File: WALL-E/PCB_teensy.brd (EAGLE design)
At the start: 92.8 x 115.8 mm, 44 parts

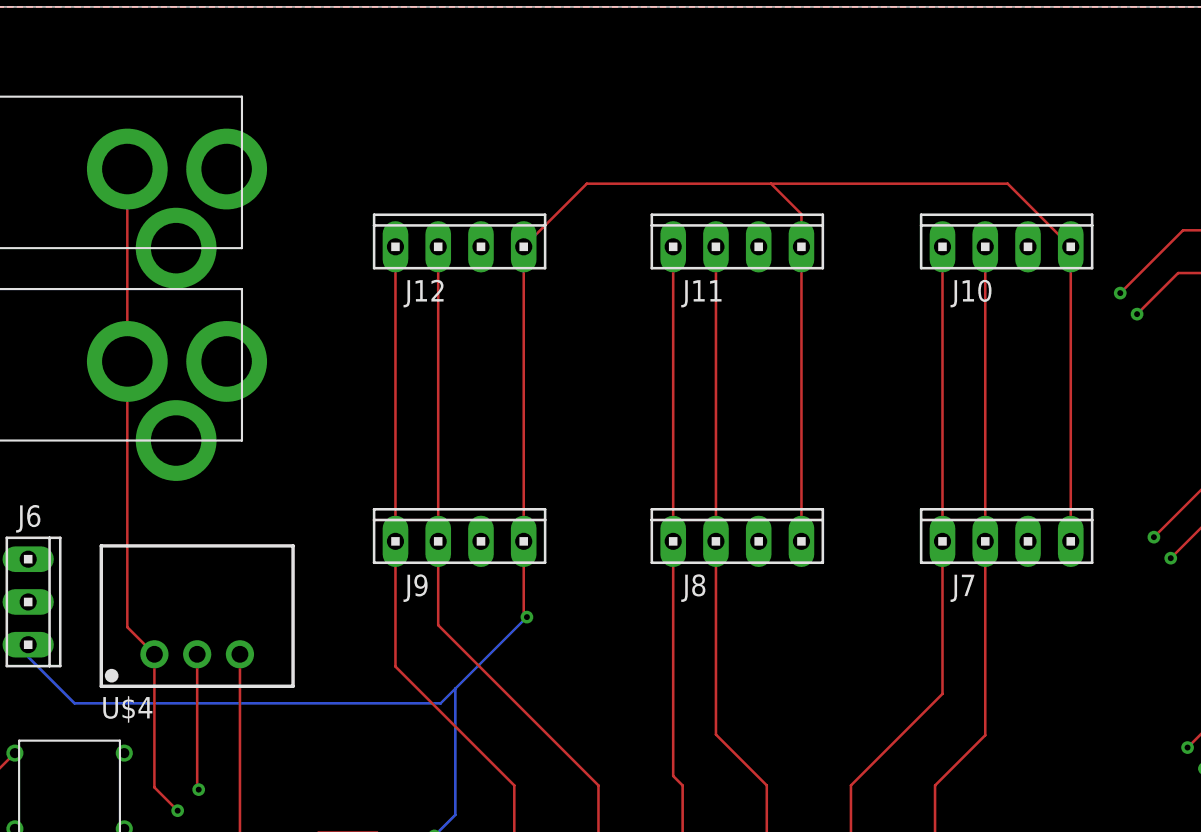
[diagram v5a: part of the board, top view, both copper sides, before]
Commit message: added silkscreen to i2c headers
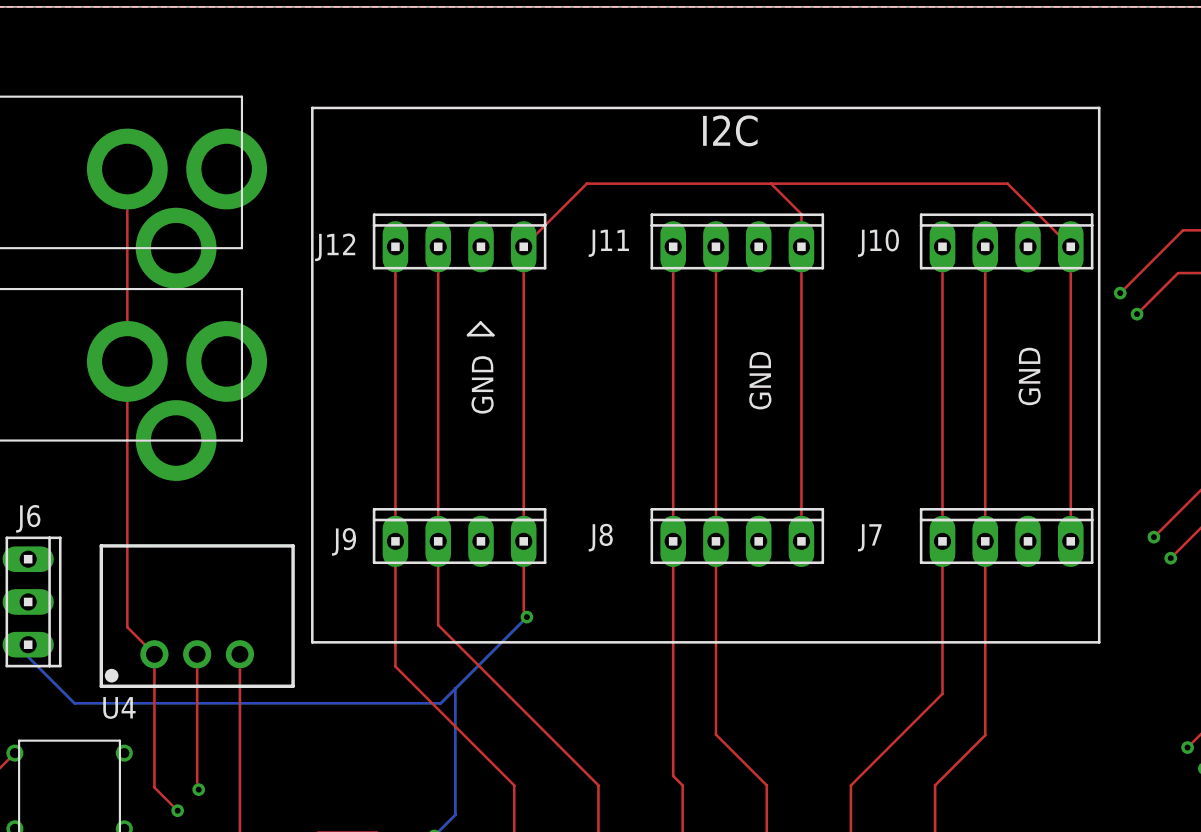
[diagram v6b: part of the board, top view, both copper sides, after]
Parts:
- renumbered U$4 to U4
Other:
- board text added: "I2C"
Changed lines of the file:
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@@
 <text x="4" y="81" size="1.016" layer="21" rot="R180">GND</text>
 <text x="4" y="78.25" size="1.016" layer="21" rot="R180">3.3V</text>
+<wire x1="70" y1="109.75" x2="70" y2="78" width="0.1524" layer="21"/>
+<wire x1="70" y1="78" x2="23.25" y2="78" width="0.1524" layer="21"/>
+<wire x1="23.25" y1="78" x2="23.25" y2="109.75" width="0.1524" layer="21"/>
+<wire x1="23.25" y1="109.75" x2="70" y2="109.75" width="0.1524" layer="21"/>
+<text x="46.25" y="107.5" size="1.778" layer="21">I2C</text>
+<text x="34" y="91.5" size="1.27" layer="21" rot="R90">GND</text>
+<text x="50.5" y="91.75" size="1.27" layer="21" rot="R90">GND</text>
+<text x="66.5" y="92" size="1.27" layer="21" rot="R90">GND</text>
+<wire x1="32.5" y1="96.25" x2="33.25" y2="97" width="0.1524" layer="21"/>
+<wire x1="33.25" y1="97" x2="34" y2="96.25" width="0.1524" layer="21"/>
+<wire x1="34" y1="96.25" x2="32.5" y2="96.25" width="0.1524" layer="21"/>
 </plain>
 <attributes>
@@
 <element name="C5" library="adafruit" library_urn="urn:adsk.eagle:library:420" package="C0805" value="" x="37.25" y="51.25" rot="R180"/>
 <element name="J1" library="con-amp" library_urn="urn:adsk.eagle:library:127" package="10X04MTA" value="" x="86.75" y="103.75" rot="R90"/>
-<element name="J10" library="con-amp" library_urn="urn:adsk.eagle:library:127" package="10X04MTA" value="" x="64.5" y="101.5"/>
-<element name="J11" library="con-amp" library_urn="urn:adsk.eagle:library:127" package="10X04MTA" value="" x="48.5" y="101.5"/>
-<element name="J12" library="con-amp" library_urn="urn:adsk.eagle:library:127" package="10X04MTA" value="" x="32" y="101.5"/>
+<element name="J10" library="con-amp" library_urn="urn:adsk.eagle:library:127" package="10X04MTA" value="" x="64.5" y="101.5" smashed="yes">
+<attribute name="NAME" x="55.7488" y="101.2488" size="1.27" layer="25"/>
+<attribute name="VALUE" x="59.5239" y="103.6509" size="1.27" layer="27"/>
+</element>
+<element name="J11" library="con-amp" library_urn="urn:adsk.eagle:library:127" package="10X04MTA" value="" x="48.5" y="101.5" smashed="yes">
+<attribute name="NAME" x="39.7488" y="101.2488" size="1.27" layer="25"/>
+<attribute name="VALUE" x="43.5239" y="103.6509" size="1.27" layer="27"/>
+</element>
+<element name="J12" library="con-amp" library_urn="urn:adsk.eagle:library:127" package="10X04MTA" value="" x="32" y="101.5" smashed="yes">
+<attribute name="NAME" x="23.4988" y="100.9988" size="1.27" layer="25"/>
+<attribute name="VALUE" x="27.0239" y="103.6509" size="1.27" layer="27"/>
+</element>
 <element name="J14" library="con-amp" library_urn="urn:adsk.eagle:library:127" package="10X04MTA" value="" x="86.75" y="61.75" rot="R90"/>
 <element name="J2" library="con-amp" library_urn="urn:adsk.eagle:library:127" package="10X04MTA" value="" x="86.75" y="89.75" rot="R90"/>
@@
 <attribute name="VALUE" x="8.5209" y="84.1762" size="1.27" layer="27" rot="R270"/>
 </element>
-<element name="J7" library="con-amp" library_urn="urn:adsk.eagle:library:127" package="10X04MTA" value="" x="64.5" y="84"/>
-<element name="J8" library="con-amp" library_urn="urn:adsk.eagle:library:127" package="10X04MTA" value="" x="48.5" y="84"/>
-<element name="J9" library="con-amp" library_urn="urn:adsk.eagle:library:127" package="10X04MTA" value="" x="32" y="84"/>
+<element name="J7" library="con-amp" library_urn="urn:adsk.eagle:library:127" package="10X04MTA" value="" x="64.5" y="84" smashed="yes">
+<attribute name="NAME" x="55.7488" y="83.7488" size="1.27" layer="25"/>
+<attribute name="VALUE" x="59.5239" y="86.1509" size="1.27" layer="27"/>
+</element>
+<element name="J8" library="con-amp" library_urn="urn:adsk.eagle:library:127" package="10X04MTA" value="" x="48.5" y="84" smashed="yes">
+<attribute name="NAME" x="39.7488" y="83.7488" size="1.27" layer="25"/>
+<attribute name="VALUE" x="43.5239" y="86.1509" size="1.27" layer="27"/>
+</element>
+<element name="J9" library="con-amp" library_urn="urn:adsk.eagle:library:127" package="10X04MTA" value="" x="32" y="84" smashed="yes">
+<attribute name="NAME" x="24.4988" y="83.4988" size="1.27" layer="25"/>
+<attribute name="VALUE" x="27.0239" y="86.1509" size="1.27" layer="27"/>
+</element>
 <element name="JP1" library="adafruit" library_urn="urn:adsk.eagle:library:420" package="1X20" value="" x="35.5" y="8.75" smashed="yes">
 <attribute name="VALUE" x="10.1" y="5.575" size="1.27" layer="27"/>
@@
 <element name="U$2" library="WALL-E_Parts" package="1825910-7" value="TACTILE-SWITCH-1825910-7" x="5.83" y="66.17" smashed="yes"/>
 <element name="U$3" library="adafruit" library_urn="urn:adsk.eagle:library:420" package="PJ-102A" value="2.1MMJACKTHM" x="8.87" y="94.59" smashed="yes" rot="R90"/>
-<element name="U$4" library="WALL-E_Parts" package="SIP3" value="R-78E5.0-0.5" x="16.41" y="77.29"/>
+<element name="U4" library="WALL-E_Parts" package="SIP3" value="R-78E5.0-0.5" x="16.41" y="77.29"/>
 <element name="U$5" library="WALL-E_Parts" package="SOT223" value="LM3940" x="25.36" y="62.58" smashed="yes">
 <attribute name="VALUE" x="22.07" y="56.2592" size="1.27" layer="27"/>
@@
 <signal name="+12V">
 <contactref element="U$6" pad="RING"/>
-<contactref element="U$4" pad="1"/>
+<contactref element="U4" pad="1"/>
 <contactref element="TP1" pad="TP"/>
 <contactref element="U$3" pad="RING"/>
@@
 </signal>
 <signal name="5V">
-<contactref element="U$4" pad="3"/>
+<contactref element="U4" pad="3"/>
 <contactref element="U$5" pad="1"/>
 <contactref element="C1" pad="1"/>
@@
 </signal>
 <signal name="N$1">
-<contactref element="U$4" pad="2"/>
+<contactref element="U4" pad="2"/>
 <contactref element="C4" pad="1"/>
 <contactref element="TP13" pad="TP"/>
